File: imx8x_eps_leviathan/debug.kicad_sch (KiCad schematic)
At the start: 77 parts, among them U19 CAT93C66VI-GT3, U20 FT2232HL, U21 LP38693MP-ADJ/NOPB, U22 TXS0101DCKR, U23 TXS0101DCKR, Y1 12MHz

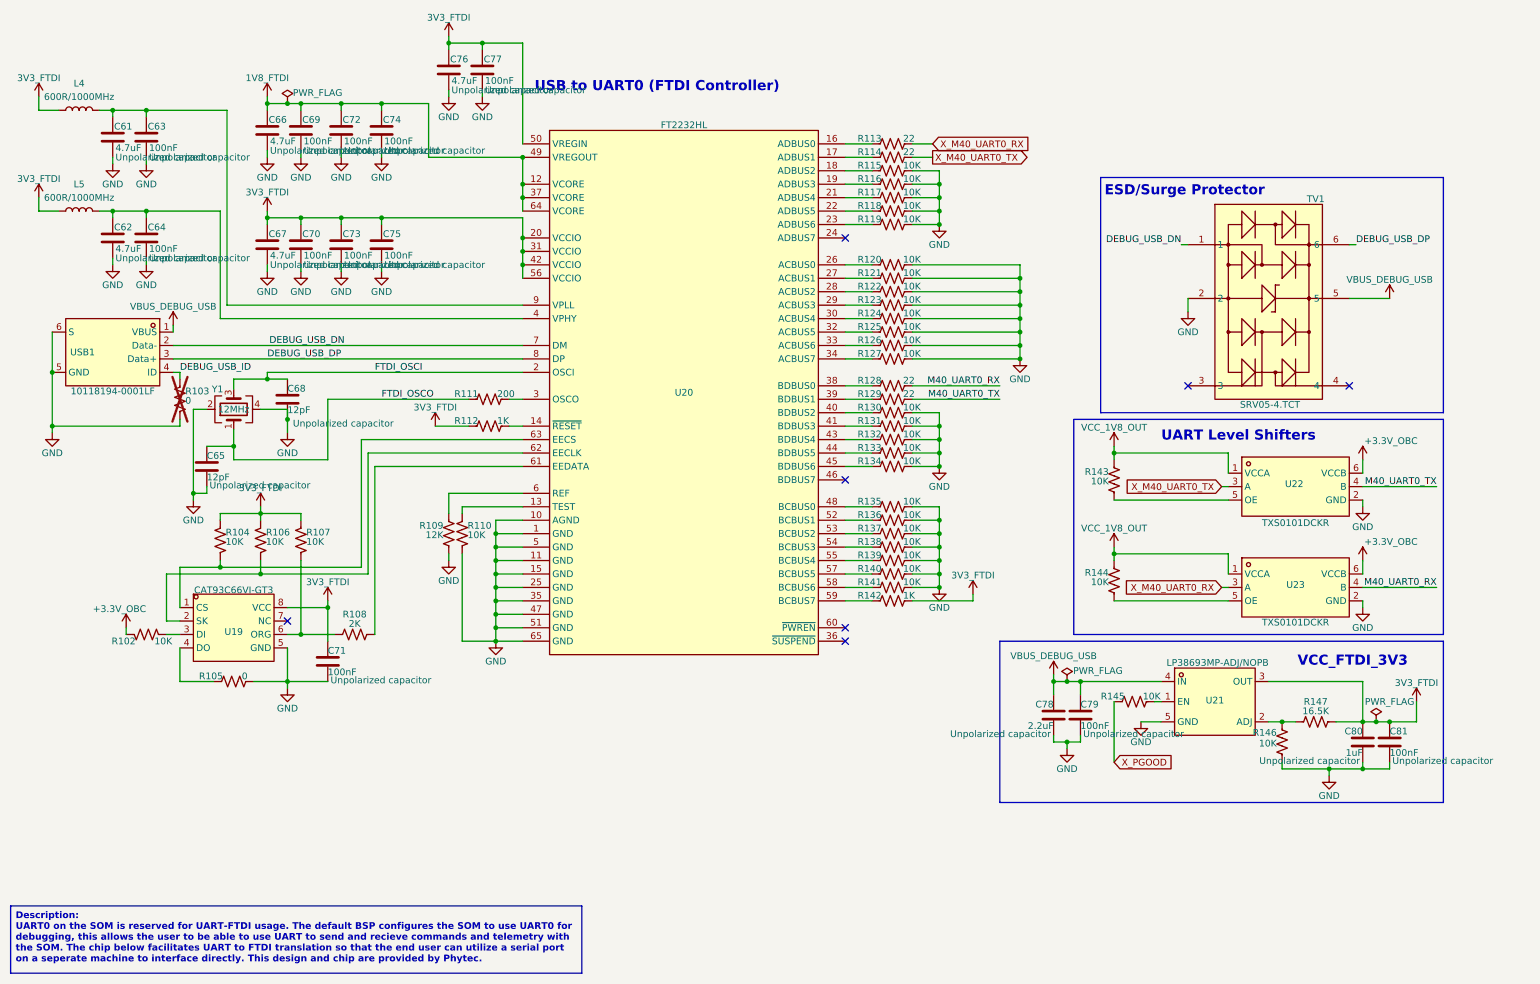
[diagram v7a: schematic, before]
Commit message: Fixed the changes from Phytec
Fixed the issues from the most recent phytec review. Need to still go through the older fixes before the board was merged. This is currently up to date for the what I think is the minimum configuration and use ability.

Thing to note is that there is still a few different sheets that I think need to be added but the major functinallity is there.
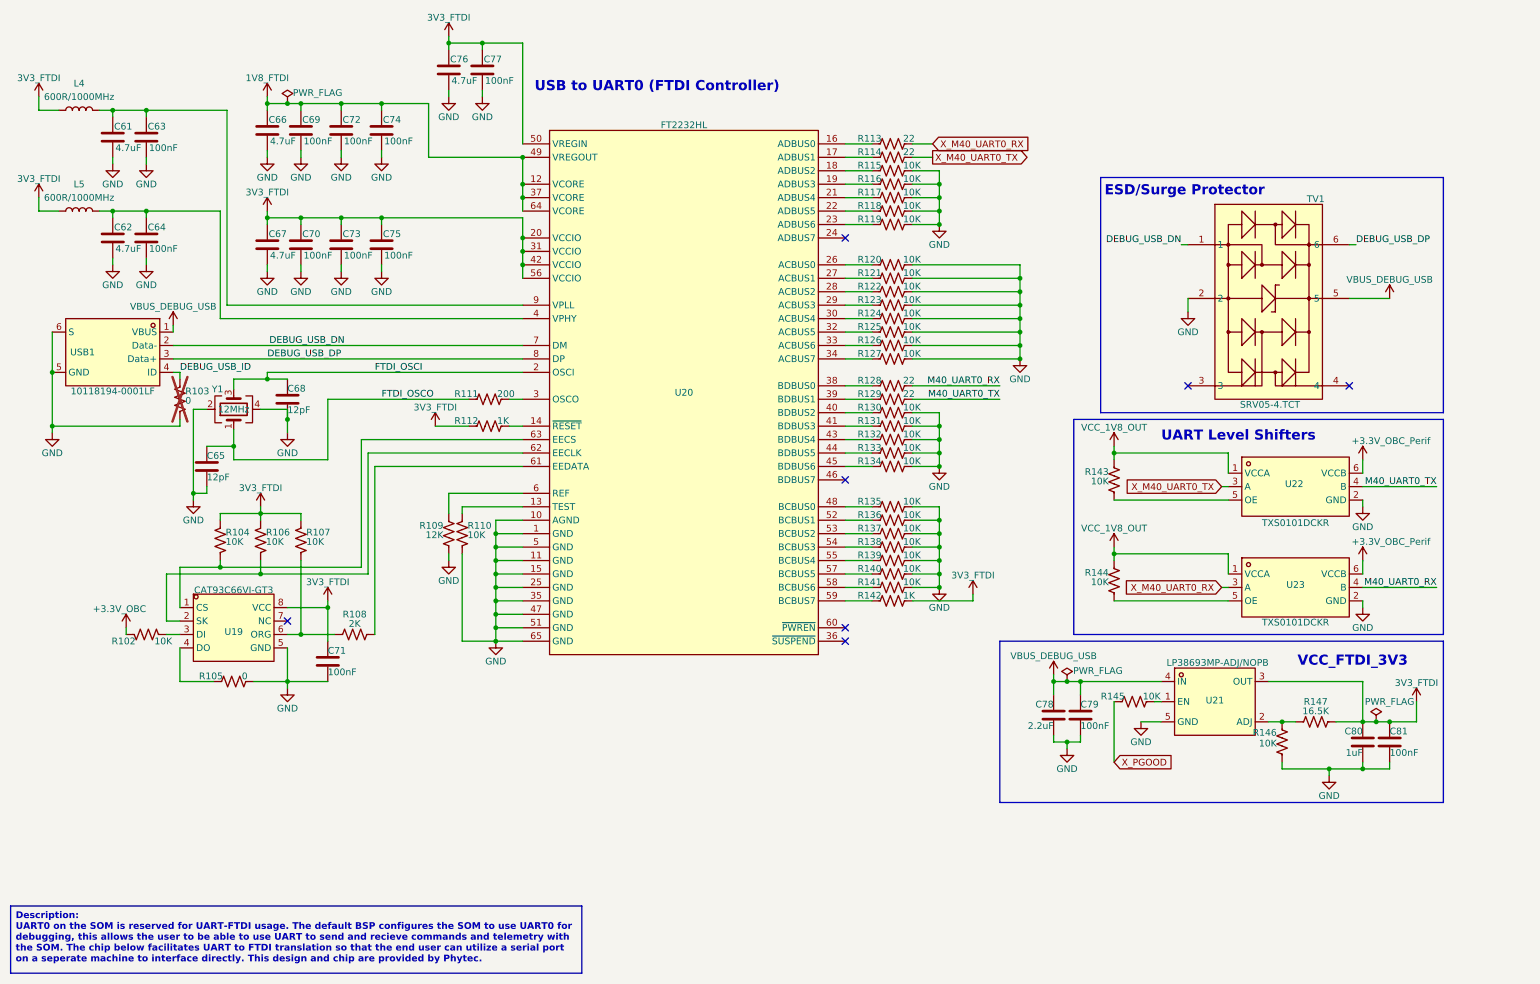
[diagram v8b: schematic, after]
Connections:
- net +3.3V_OBC: no longer U22.6 (VCCB), U23.6 (VCCB)
- new net +3.3V_OBC_Perif: U22.6 (VCCB), U23.6 (VCCB)
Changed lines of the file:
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@@
 			)
 		)
-		(property "Value" "+3.3V_OBC"
+		(property "Value" "+3.3V_OBC_Perif"
 			(at 273.304 96.774 0)
 			(effects
@@
 				)
 				(justify left)
+				(hide yes)
 			)
 		)
@@
 				)
 				(justify left)
+				(hide yes)
 			)
 		)
@@
 				)
 				(justify left)
+				(hide yes)
 			)
 		)
@@
 				)
 				(justify left)
+				(hide yes)
 			)
 		)
@@
 				)
 				(justify left)
+				(hide yes)
 			)
 		)
@@
 				)
 				(justify left)
+				(hide yes)
 			)
 		)
@@
 				)
 				(justify left)
+				(hide yes)
 			)
 		)
@@
 				)
 				(justify left)
+				(hide yes)
 			)
 		)
@@
 				)
 				(justify left)
+				(hide yes)
 			)
 		)
@@
 				)
 				(justify left)
+				(hide yes)
 			)
 		)
@@
 				)
 				(justify left)
+				(hide yes)
 			)
 		)
@@
 				)
 				(justify left)
+				(hide yes)
 			)
 		)
@@
 				)
 				(justify left)
+				(hide yes)
 			)
 		)
@@
 				)
 				(justify left)
+				(hide yes)
 			)
 		)
@@
 			)
 		)
-		(property "Value" "+3.3V_OBC"
+		(property "Value" "+3.3V_OBC_Perif"
 			(at 273.304 115.824 0)
 			(effects
@@
 				)
 				(justify left)
+				(hide yes)
 			)
 		)
@@
 				)
 				(justify left)
+				(hide yes)
 			)
 		)
@@
 				)
 				(justify left)
+				(hide yes)
 			)
 		)
@@
 				)
 				(justify left)
+				(hide yes)
 			)
 		)
@@
 				)
 				(justify left)
+				(hide yes)
 			)
 		)
@@
 				)
 				(justify left)
+				(hide yes)
 			)
 		)
@@
 				)
 				(justify left)
+				(hide yes)
 			)
 		)
